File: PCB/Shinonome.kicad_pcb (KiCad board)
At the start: 2 copper layers, 127.7 x 87.9 mm, 44 parts, among them J1 MJ-4PP-9, SW1 SW_PUSH, SW10 SW_PUSH, SW11 SW_PUSH, SW12 SW_PUSH, SW13 SW_PUSH, SW14 SW_PUSH, SW15 SW_PUSH, SW16 SW_PUSH, SW17 SW_PUSH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

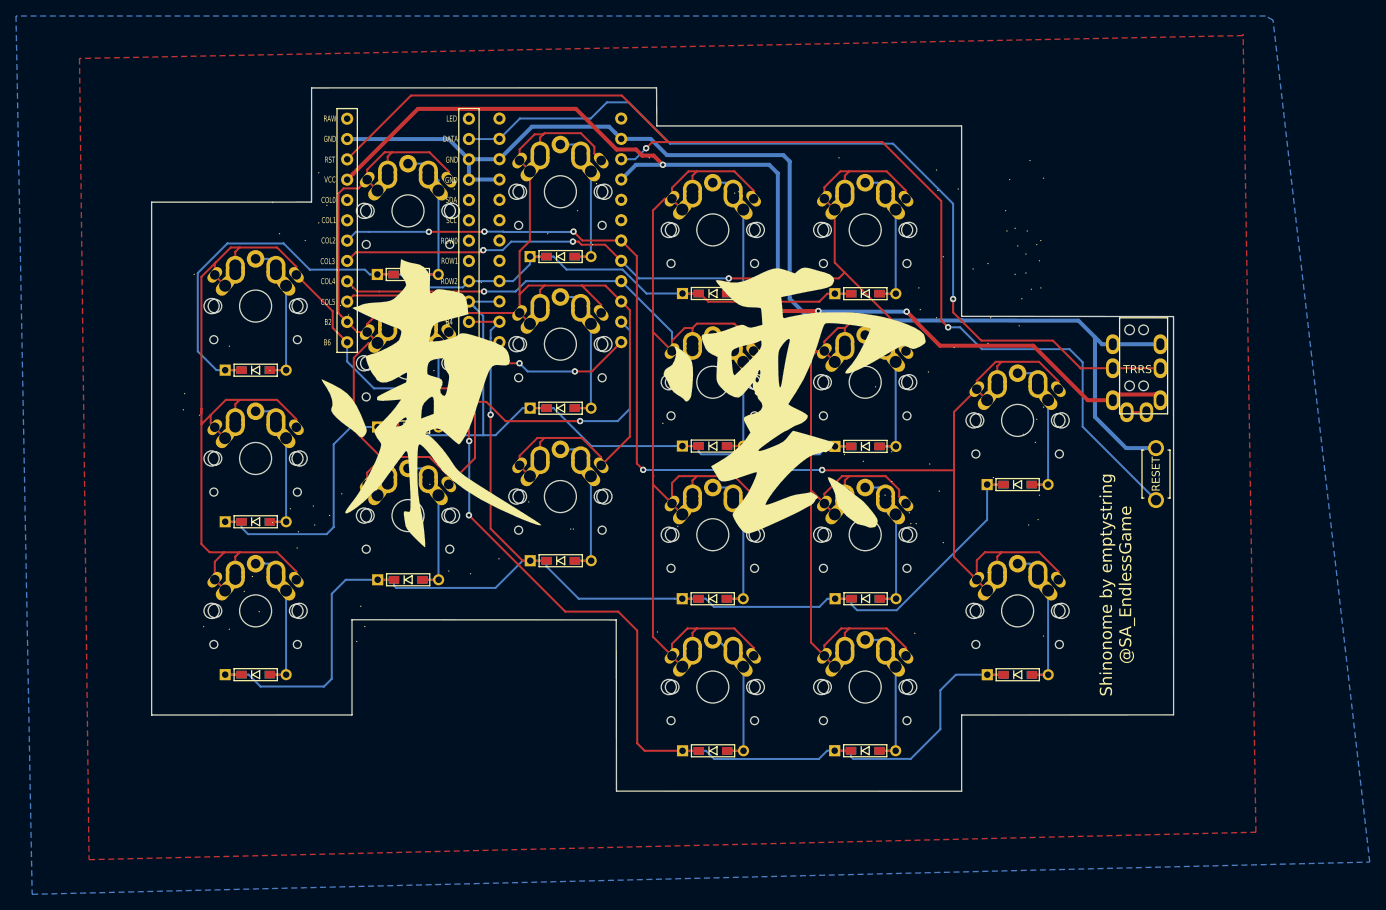
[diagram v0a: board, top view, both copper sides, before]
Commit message: fixed trrs jack incorrect pins
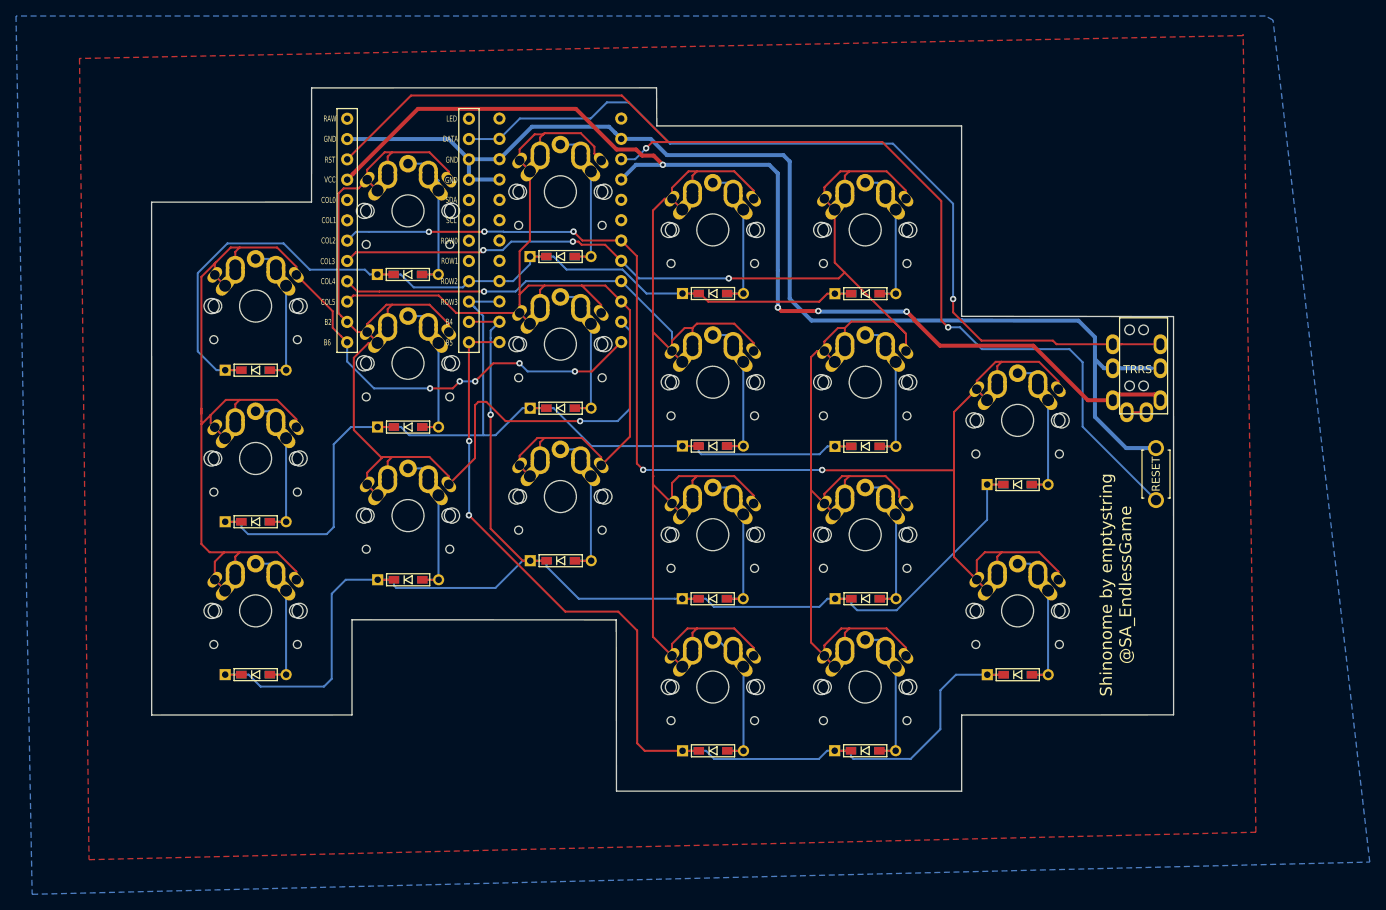
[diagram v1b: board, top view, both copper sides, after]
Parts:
- removed G***: LOGO, Shinonome:kanji
- removed G***: LOGO, Shinonome:emptystringLogo
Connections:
- J1 pad B: GND -> data
- J1 pad C: data -> GND
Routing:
- net data: track 110.2 -> 108.8 mm
- net GND: track 151.3 -> 151.8 mm

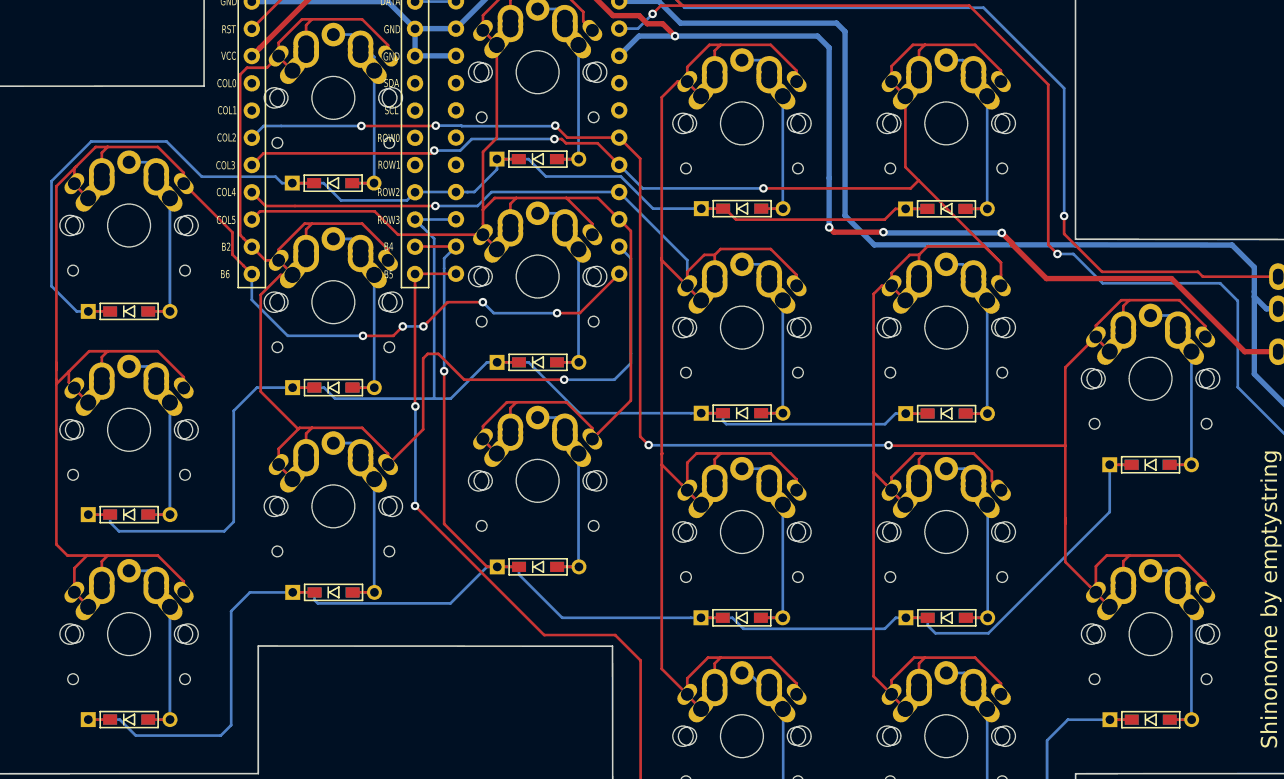
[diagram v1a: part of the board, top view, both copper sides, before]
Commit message: added logos and regenerated gerber
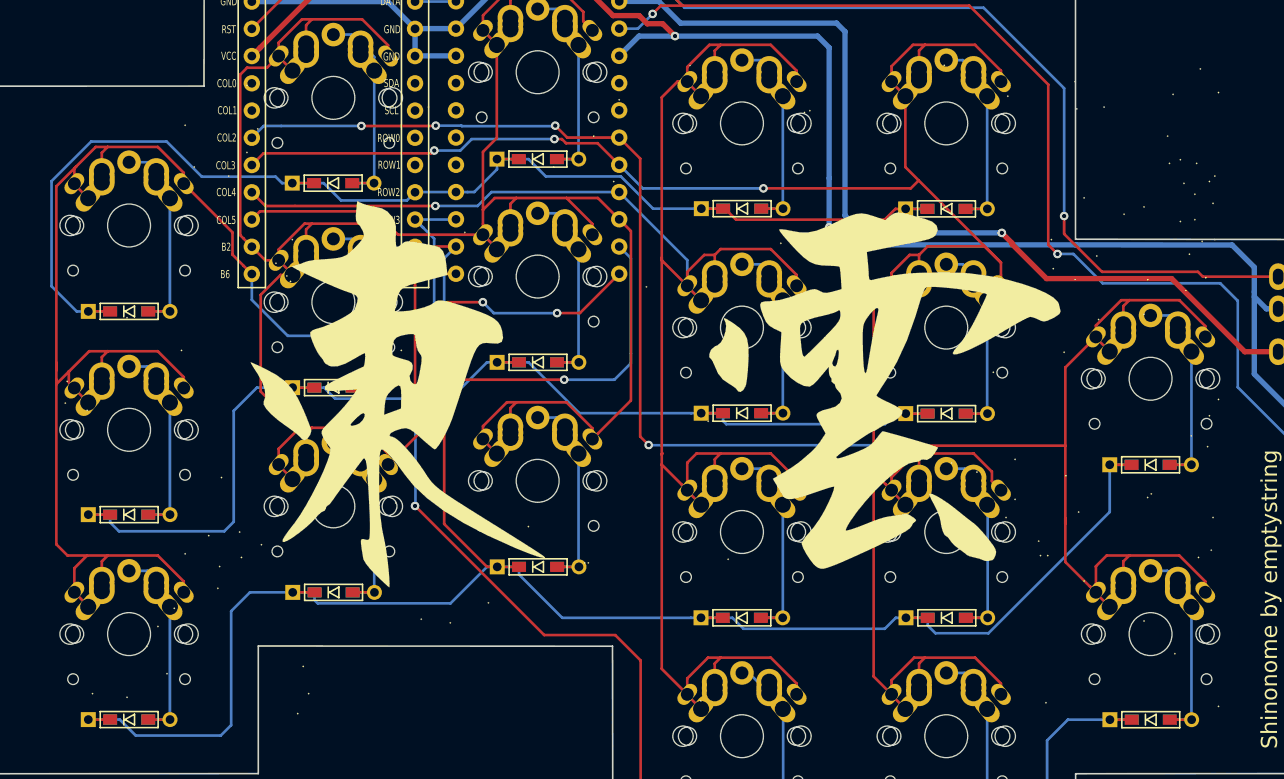
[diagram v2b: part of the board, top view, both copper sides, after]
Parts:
- added G***: LOGO, Shinonome:emptystringLogo, B.Cu at (142.4, 121.9)
- added G***: LOGO, Shinonome:kanji, F.Cu at (150.2, 111.0)
